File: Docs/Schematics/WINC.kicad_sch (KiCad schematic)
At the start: 4 parts, among them U1 ATWINC1500-MR, U2 RFBPB2012090A9T

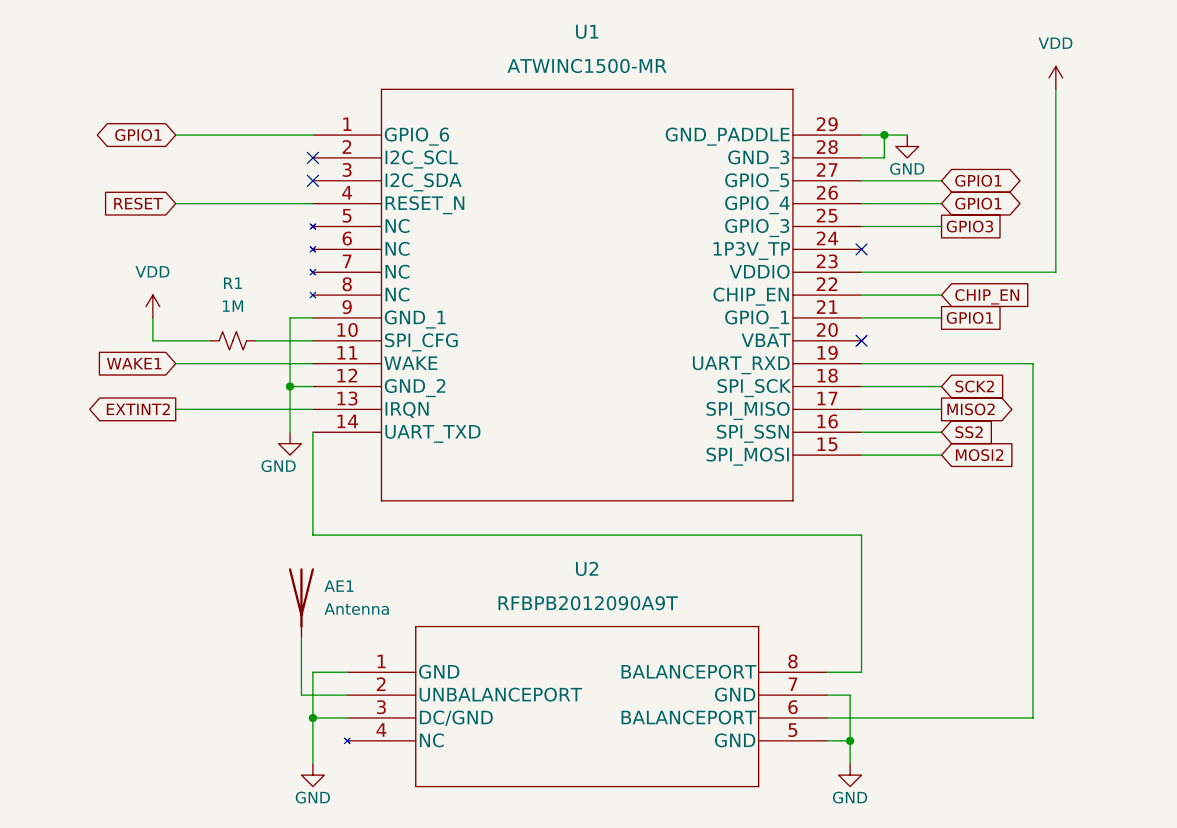
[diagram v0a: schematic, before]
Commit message: Revision 2
Fixes based after sponsor interview.
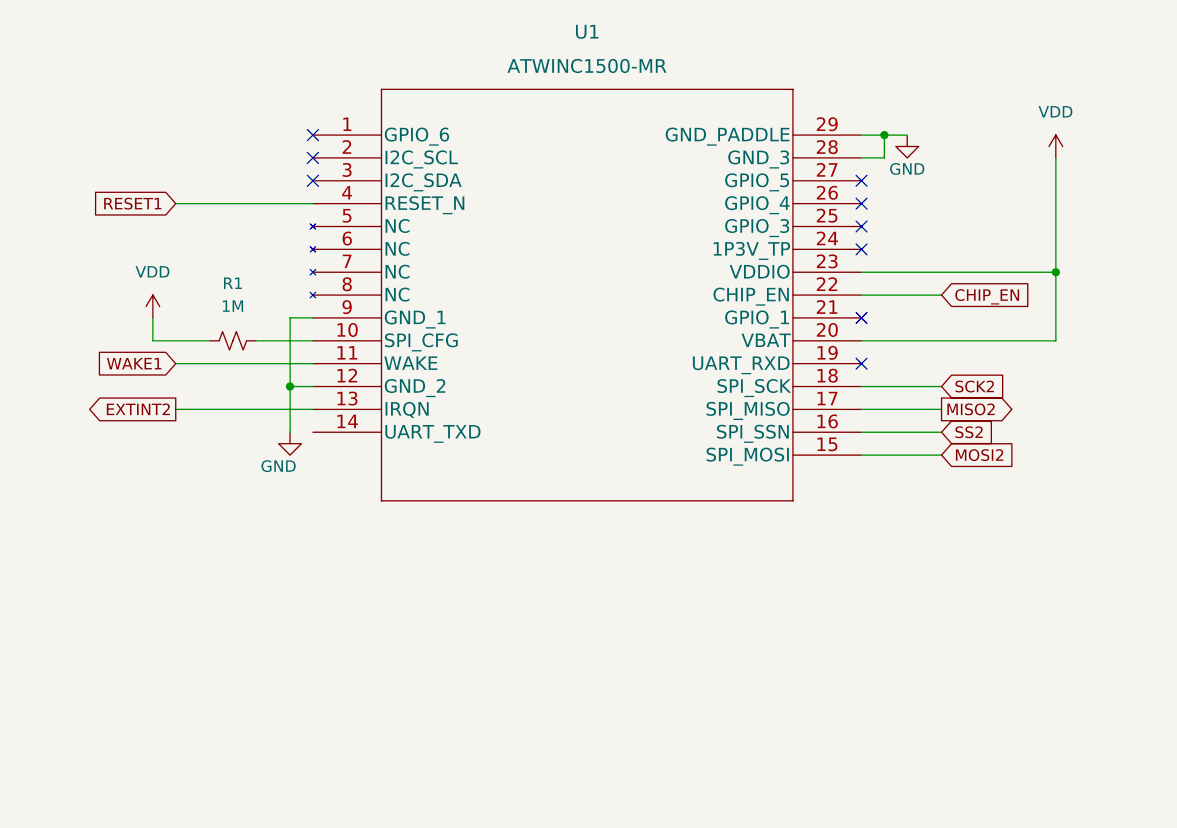
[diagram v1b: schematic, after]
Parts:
- removed AE1: Antenna, symbol Device:Antenna
- removed U2: RFBPB2012090A9T, LTCC-8_2P0X1P2_WAL, symbol RFBPB2012090A9T:RFBPB2012090A9T
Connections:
- net VDD: now also U1.20 (VBAT)
- removed net GPIO1: U1.1 (GPIO_6), U1.21 (GPIO_1), U1.26 (GPIO_4), U1.27 (GPIO_5)
- net GPIO3: no longer names the net of U1.25 (GPIO_3)
- net RESET renamed RESET1
- no-connect marks 4 -> 9

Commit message: Revision 3
Revisions made after meeting with sponsor.
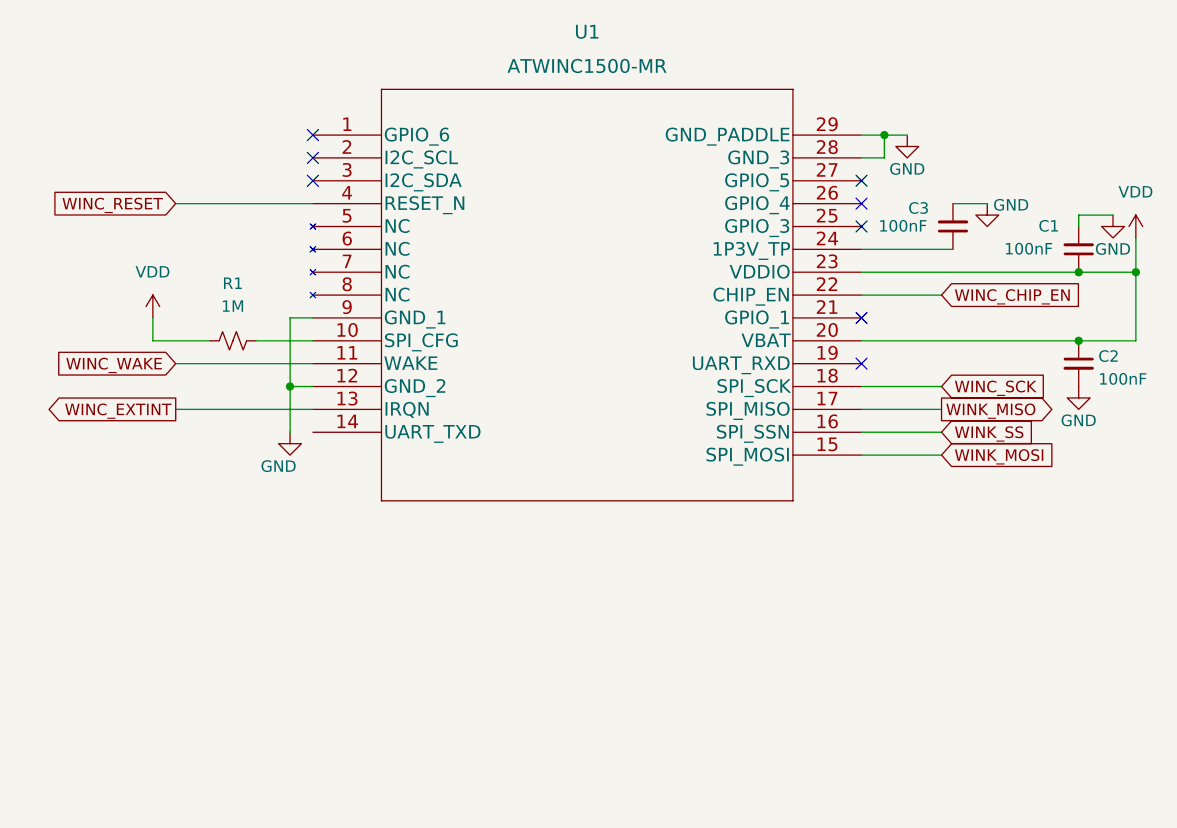
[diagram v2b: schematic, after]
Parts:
- added C1, C2, C3: 100nF, symbol Device:C_Small
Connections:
- net GND: now also C1.2, C2.2, C3.2
- net VDD: now also C1.1, C2.1
- net at U1.24 (1P3V_TP): now also C3.1
- net CHIP_EN renamed WINC_CHIP_EN
- net EXTINT2 renamed WINC_EXTINT
- net MISO2 renamed WINK_MISO
- net MOSI2 renamed WINK_MOSI
- net RESET1 renamed WINC_RESET
- net SCK2 renamed WINC_SCK
- net SS2 renamed WINK_SS
- net WAKE1 renamed WINC_WAKE
- no-connect marks 9 -> 8
